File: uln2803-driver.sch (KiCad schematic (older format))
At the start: 10 parts, among them K1 BAT, P1 IN1, P2 IN2, P3 IN3, P4 IN4, P5 OUT1, P6 OUT2, P7 OUT3, P8 OUT4, U1 ULN2803

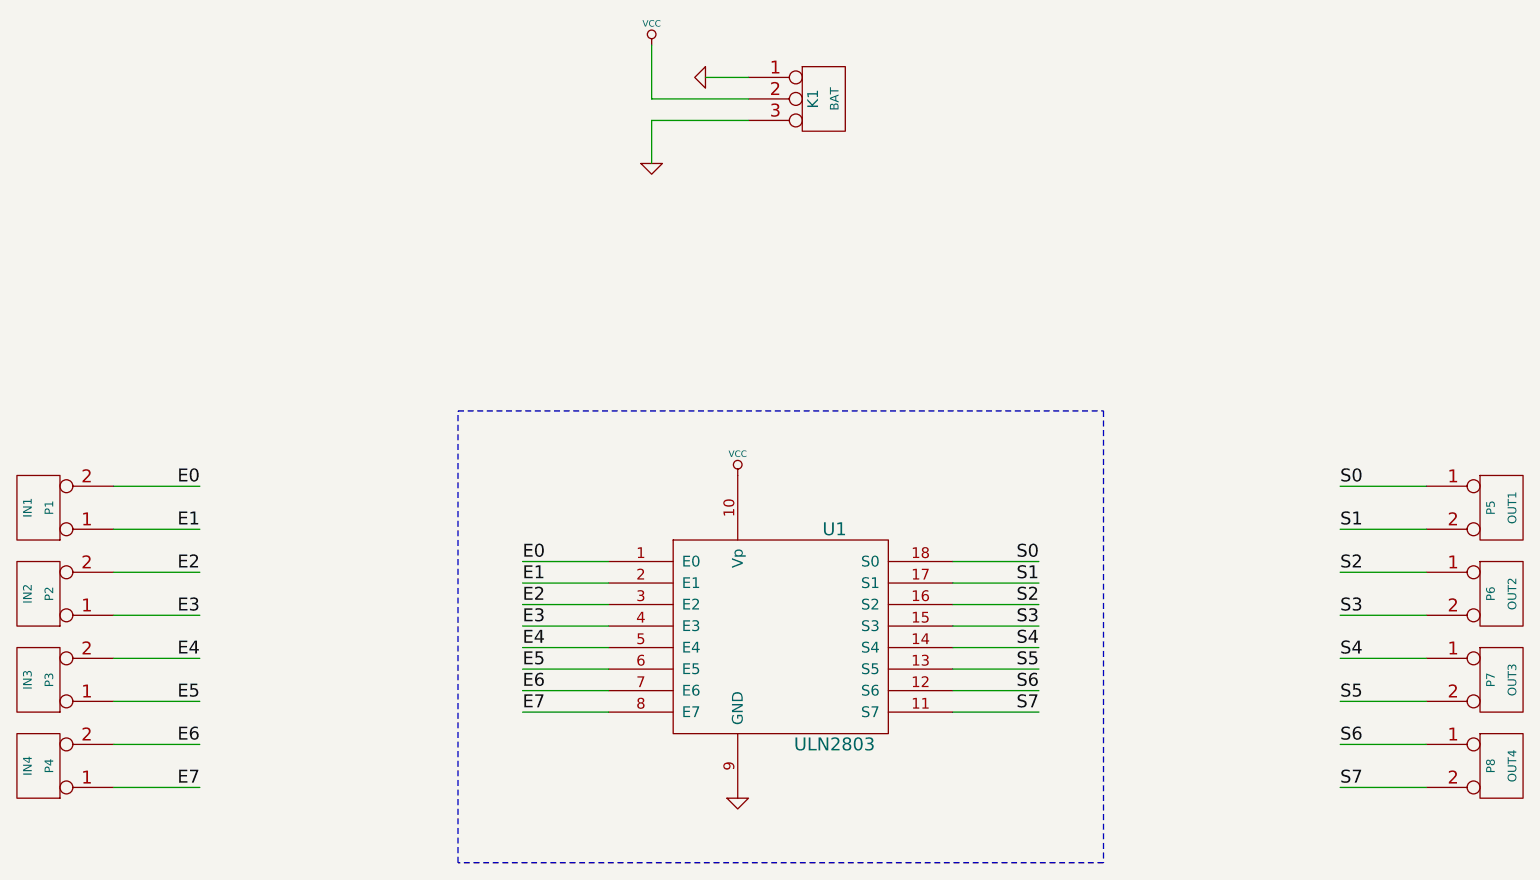
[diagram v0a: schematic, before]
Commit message: Changed borniers from mpt with 2,54mm pitch to mkds with 5mm pitch. Added filled zones to connect GND.
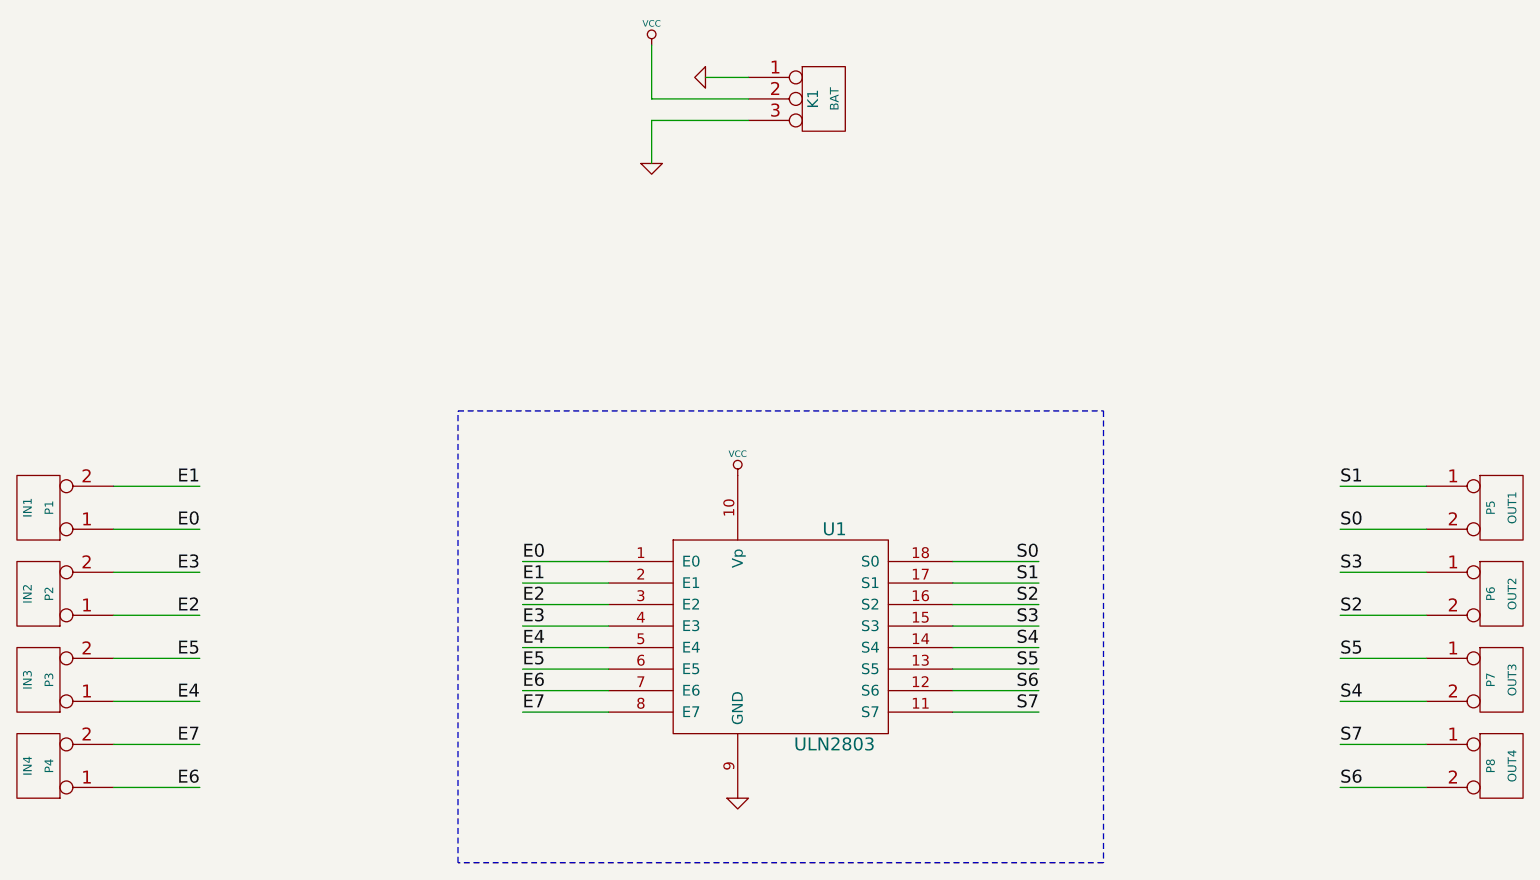
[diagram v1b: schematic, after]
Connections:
- net E0: now also P1.1 (P1); no longer P1.2 (PM)
- net E1: now also P1.2 (PM); no longer P1.1 (P1)
- net E2: now also P2.1 (P1); no longer P2.2 (PM)
- net E3: now also P2.2 (PM); no longer P2.1 (P1)
- net E4: now also P3.1 (P1); no longer P3.2 (PM)
- net E5: now also P3.2 (PM); no longer P3.1 (P1)
- net E6: now also P4.1 (P1); no longer P4.2 (PM)
- net E7: now also P4.2 (PM); no longer P4.1 (P1)
- net S0: now also P5.2 (PM); no longer P5.1 (P1)
- net S1: now also P5.1 (P1); no longer P5.2 (PM)
- net S2: now also P6.2 (PM); no longer P6.1 (P1)
- net S3: now also P6.1 (P1); no longer P6.2 (PM)
- net S4: now also P7.2 (PM); no longer P7.1 (P1)
- net S5: now also P7.1 (P1); no longer P7.2 (PM)
- net S6: now also P8.2 (PM); no longer P8.1 (P1)
- net S7: now also P8.1 (P1); no longer P8.2 (PM)
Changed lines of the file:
@@
-EESchema Schematic File Version 2  date sáb 01 nov 2014 20:19:26 ART
+EESchema Schematic File Version 2  date mar 04 nov 2014 21:11:13 ART
 LIBS:power
 LIBS:device
@@
 Sheet 1 1
 Title "ULN2803 Driver"
-Date "1 nov 2014"
+Date "5 nov 2014"
 Rev "1.0"
 Comp "Victor Villarreal"
@@
 	-1   0    0    1
 $EndComp
+Text Label 3000 3850 2    60   ~ 0
+E0
 Text Label 3000 3650 2    60   ~ 0
-E0
-Text Label 3000 3850 2    60   ~ 0
 E1
+Text Label 3000 4250 2    60   ~ 0
+E2
 Text Label 3000 4050 2    60   ~ 0
-E2
-Text Label 3000 4250 2    60   ~ 0
 E3
+Text Label 3000 4650 2    60   ~ 0
+E4
 Text Label 3000 4450 2    60   ~ 0
-E4
-Text Label 3000 4650 2    60   ~ 0
 E5
+Text Label 3000 5050 2    60   ~ 0
+E6
 Text Label 3000 4850 2    60   ~ 0
-E6
-Text Label 3000 5050 2    60   ~ 0
 E7
 $Comp
@@
 	1    0    0    -1
 $EndComp
+Text Label 8300 3850 0    60   ~ 0
+S0
 Text Label 8300 3650 0    60   ~ 0
-S0
-Text Label 8300 3850 0    60   ~ 0
 S1
+Text Label 8300 4250 0    60   ~ 0
+S2
 Text Label 8300 4050 0    60   ~ 0
-S2
-Text Label 8300 4250 0    60   ~ 0
 S3
+Text Label 8300 4650 0    60   ~ 0
+S4
 Text Label 8300 4450 0    60   ~ 0
-S4
-Text Label 8300 4650 0    60   ~ 0
 S5
+Text Label 8300 5050 0    60   ~ 0
+S6
 Text Label 8300 4850 0    60   ~ 0
-S6
-Text Label 8300 5050 0    60   ~ 0
 S7
 $Comp
